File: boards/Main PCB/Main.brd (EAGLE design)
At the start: 160 x 101.3 mm, 19 parts, among them IC2 CP210X_USB_UART, X1 USB-MICROB

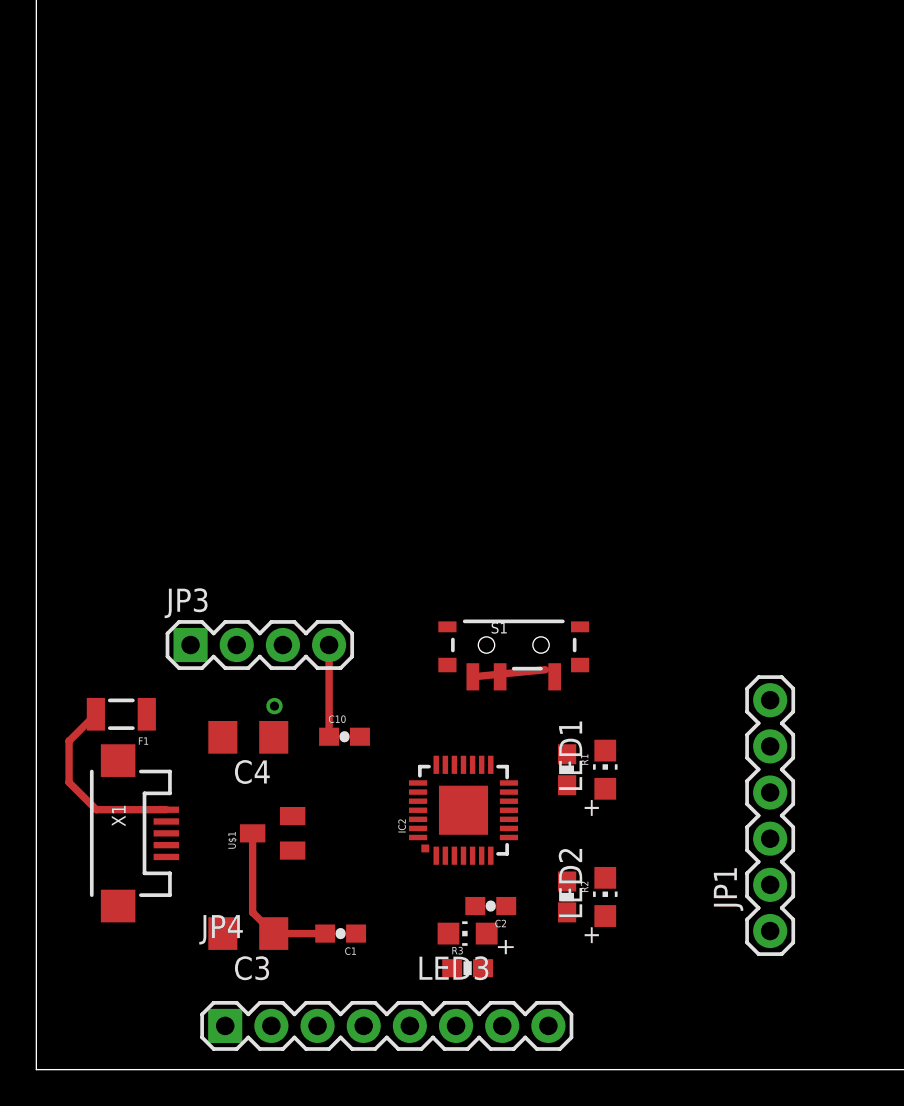
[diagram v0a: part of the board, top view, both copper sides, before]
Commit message: Adding miniusb UART converter and updating main to include IMU
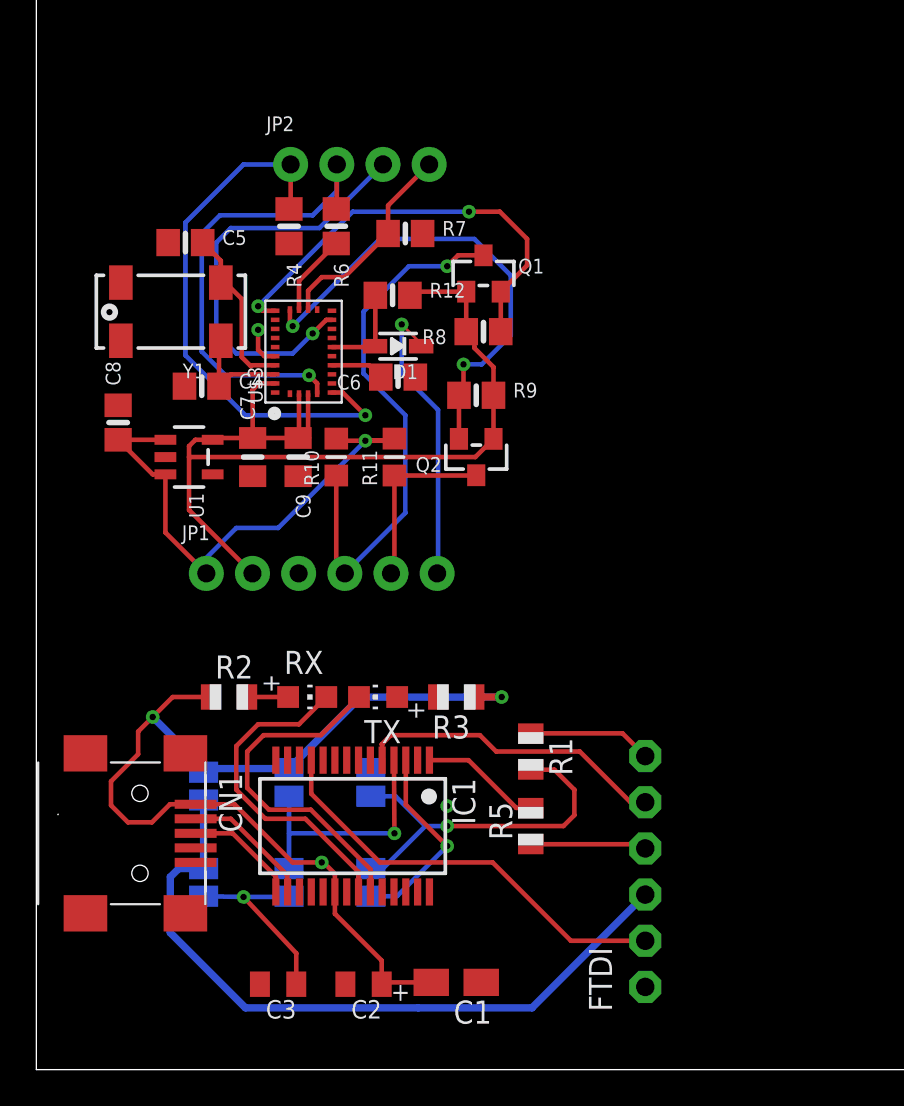
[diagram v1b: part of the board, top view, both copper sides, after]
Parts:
- removed C10: 100nF, SparkFun:0603-CAP
- removed F1: PTCSMD, SparkFun:PTC-1206
- removed IC2: CP210X_USB_UART, SparkFun-DigitalIC:MLP28
- removed JP3: (no value), SparkFun:1X04
- removed JP4: (no value), SparkFun:1X08
- removed LED1: bijela, adafruit:CHIP-LED0805
- removed LED2: crvena, adafruit:CHIP-LED0805
- removed LED3: plava, adafruit:CHIP-LED0805
- removed S1: (no value), SparkFun:SWITCH-SPST-SMD-A
- removed U$1: 622K, SparkFun:662K
- removed X1: USB-MICROB, SparkFun:USB-MICROB
- added C5: 22pF, microbuilder:0805-NO
- added C6: 0.1uF, microbuilder:0805-NO
- added C7: 0.1uF, microbuilder:0805_10MGAP
- added C8: 10uF, microbuilder:0805-NO
- added C9: 10uF, microbuilder:0805_10MGAP
- added CN1: MINIB, adafruit:USB-MINIB
- added D1: 1n4148, microbuilder:SOD-323
- added FTDI: (no value), adafruit:1X06-CLEANBIG
- added IC1: FT232RL, ftdichip:SSOP28
- added JP2: (no value), microbuilder:1X04_ROUND_76
- added Q1, Q2: BSS138, microbuilder:SOT23-WIDE
- added R10, R11: 10K, microbuilder:_0805MP
- added R12, R4, R6, R7, R8, R9: 10K, microbuilder:0805-NO
- added R5: 10, adafruit:R0805
- added RX: Green, adafruit:CHIP-LED0805
- added SJ1, SJ2, SJ3, SJ4, SJ5, SJ6: (no value), jumper:SJ
- added TX: Red, adafruit:CHIP-LED0805
- added U$3: BNO055, microbuilder:BNO055
- added U1: MIC5225-3.3, microbuilder:SOT23-5
- added Y1: 32.768kHz, microbuilder:CRYSTAL_8X3.8
- C1: value 100nF -> 10uF; device SparkFun:0603-CAP -> adafruit:A/3216-18R
- C2: value 100nF -> 0.1uF; device SparkFun:0603-CAP -> adafruit:C0805K
- C3: value 10uF -> 0.1uF; device rcl:C3216 -> adafruit:C0805K
- C4: value 22uF -> 22pF; device rcl:C3216 -> microbuilder:0805-NO
- JP1: value FTDI_BASICPTH -> (none); device SparkFun:FTDI_BASIC -> microbuilder:1X06_ROUND_76
- R1: value 680 -> 10; device SparkFun:0603-RES -> adafruit:R0805
- R2, R3: value 680 -> 1K; device SparkFun:0603-RES -> adafruit:R0805
- moved JP1 31.6 mm to (15.7, 27.3), turned to 0 degrees
- moved R2 21.6 mm to (10.6, 20.5), turned to 0 degrees
- moved C4 19.5 mm to (9.10, 37.6), turned to 0 degrees
- moved R3 14.9 mm to (23.1, 20.5), turned to 180 degrees
- moved C2 8.22 mm to (18.0, 4.70)
- moved C1 6.90 mm to (23.1, 4.80)
- moved C3 3.23 mm to (13.3, 4.70)
- moved R1 2.24 mm to (27.2, 17.5)
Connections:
- removed net D+: IC2.4, X1.D+
- removed net D-: IC2.5, X1.D-
- removed net DCD: IC2.1, JP4.4
- removed net DSR: IC2.27, JP4.3
- removed net RI: IC2.2, JP4.5
- removed net RST: IC2.9, JP4.8
- removed net RXD: IC2.25, JP1.RXI, LED2.C
- removed net SUSPEND: IC2.12, JP4.7
- removed net SUSPEND': IC2.11, JP4.6
- removed net TXD: IC2.26, JP1.TXO, LED1.C
- removed net VBUS: F1.2, X1.VBUS
- removed net VCC: JP1.VCC, S1.2
- new net +3V3: C3.1, IC1.17, SJ4.2, SJ5.2
- new net 5.0V: C8.1, JP1.1, R10.2, R11.2, U1.1, U1.3
- new net I2CADDR_3V: JP2.4, R7.1, U$3.17
- new net INT_3V: JP2.3, U$3.14
- new net N$10: C5.2, U$3.26, Y1.P$1
- new net N$11: C6.2, U$3.9
- new net N$5: IC1.1, R5.2
- new net N$6: IC1.23, TX.C
- new net N$7: IC1.22, RX.C
- new net N$8: R2.2, RX.A
- new net N$9: R3.2, TX.A
- new net NRESET_3V: D1.A, R12.1, U$3.11
- new net PS0_3V: JP2.1, R4.1, U$3.6
- new net PS1_3V: JP2.2, R6.1, U$3.5
- new net RST_5V: D1.C, JP1.6
- new net RTSDTR: R1.2, SJ3.2, SJ6.1
- new net RX: FTDI.5, IC1.5
- new net SCL_3V: Q2.2, R9.1, U$3.19
- new net SCL_5V: JP1.5, Q2.3, R11.1
- new net SDA_3V: Q1.2, R8.1, U$3.20
- new net SDA_5V: JP1.4, Q1.3, R10.1
- new net TX: FTDI.4, R5.1
- new net VCCIO: IC1.4, SJ2.2, SJ5.1
- new net VCCOUT: FTDI.3, SJ1.2, SJ4.1
- net +5V: now also C1.+, C2.1, CN1.VBUS, IC1.20, SJ1.1, SJ2.1; no longer C1.2, C3.1, F1.1, IC2.7, IC2.8, JP3.3, R1.1, S1.1, U$1.IN
- net 3.3V: now also C7.2, C9.1, JP1.2, Q1.1, Q2.1, R12.2, R8.2, R9.2, U$3.28, U$3.3, U$3.4, U1.5; no longer C10.1, C4.1, JP3.4, S1.3, U$1.OUT
- net CTS: now also FTDI.2, IC1.11; no longer IC2.23, JP1.CTS, JP4.1
- net DTR: now also IC1.2, SJ6.2; no longer IC2.28, JP1.DTR
- net GND: now also C1.-, C4.1, C5.1, C6.1, C7.1, C8.2, C9.2, CN1.GND, FTDI.1, IC1.18, IC1.21, IC1.25, IC1.26, IC1.7, JP1.3, R4.2, R6.2, R7.2, U$3.10, U$3.15, U$3.16, U$3.18, U$3.2, U$3.25, U1.2; no longer C1.1, C10.2, C4.2, IC2.3, IC2.EXP, IC2.M, JP1.GND, JP3.1, JP3.2, LED3.C, U$1.GND, X1.GND
- net N$1: now also C4.2, U$3.27, Y1.P$4; no longer LED1.A, R1.2
- net N$2: now also FTDI.6, R1.1; no longer LED2.A, R2.2
- net N$3: now also CN1.D+, IC1.15; no longer LED3.A, R3.2
- net N$4: now also CN1.D-, IC1.16; no longer C2.1, IC2.6
- net RTS: now also IC1.3, SJ3.1; no longer IC2.24, JP4.2
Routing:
- net 3.3V: track 5.05 -> 53.2 mm
- net +5V: track 12.8 -> 57.9 mm, vias 0 -> 3
- net VCCOUT: track 0.00 -> 39.3 mm
- net PS0_3V: track 0.00 -> 30.5 mm, vias 0 -> 1
- net SDA_5V: track 0.00 -> 30.2 mm, vias 0 -> 1
- net 5.0V: track 0.00 -> 29.2 mm, vias 0 -> 1
- net SCL_3V: track 0.00 -> 26.6 mm, vias 0 -> 2
- net PS1_3V: track 0.00 -> 26.5 mm, vias 0 -> 1
- net SDA_3V: track 0.00 -> 24.3 mm, vias 0 -> 2
- net CTS: track 0.00 -> 23.6 mm
- net INT_3V: track 0.00 -> 23.5 mm, vias 0 -> 1
- net RTSDTR: track 0.00 -> 20.4 mm, vias 0 -> 1
- net N$6: track 0.00 -> 19.3 mm
- net N$7: track 0.00 -> 18.2 mm
- net RX: track 0.00 -> 17.1 mm
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
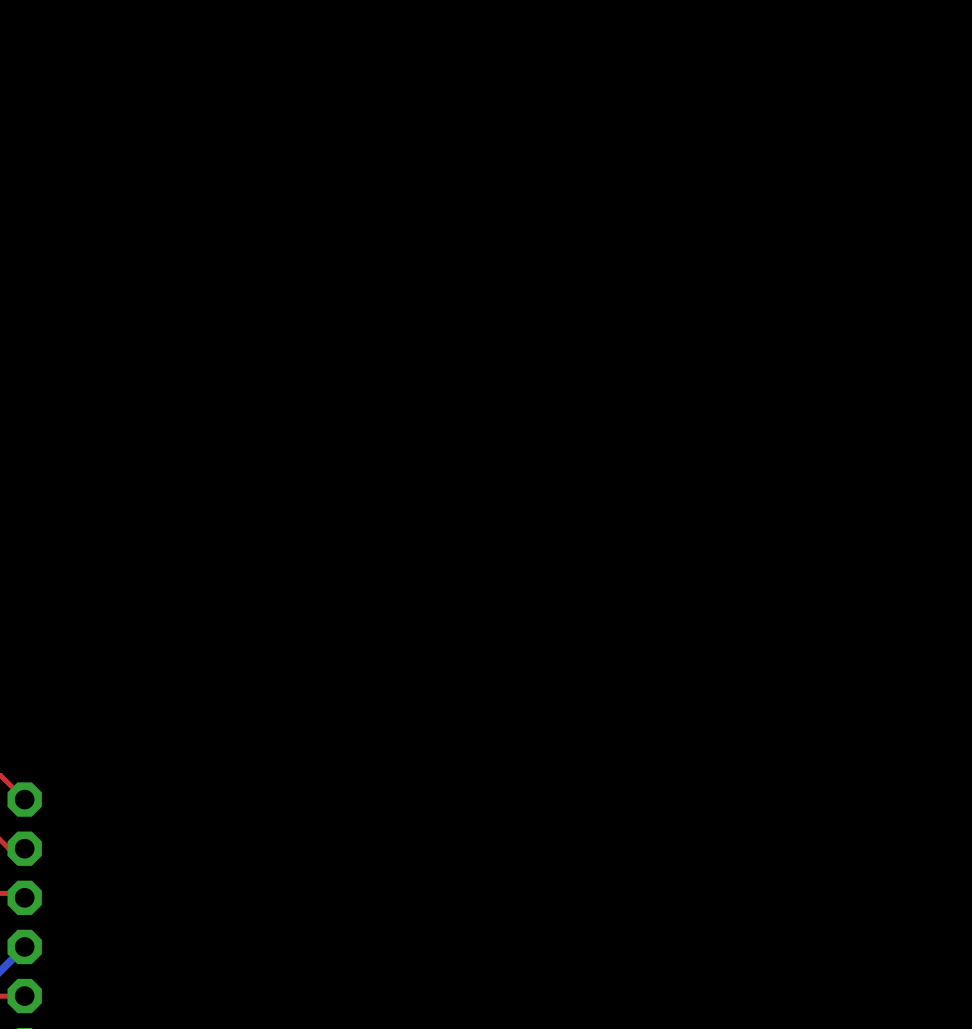
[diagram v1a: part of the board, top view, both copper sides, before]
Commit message: Fixing NS-HP-GL library and importing footprint to main PCB
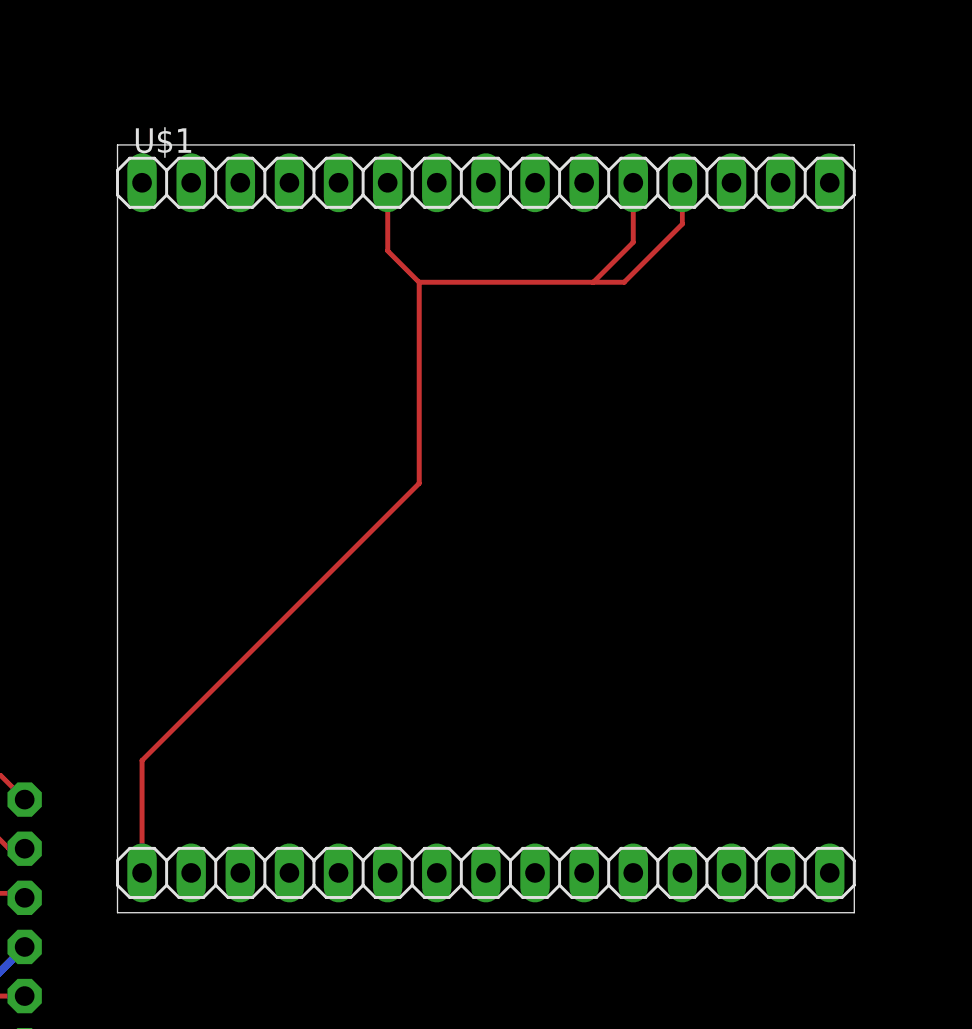
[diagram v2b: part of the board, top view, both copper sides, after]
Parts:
- added U$1: GPS, NS-HP-GL:GPS
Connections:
- new net RX1: U$1.19
- new net RX2: U$1.22
- new net TX1: U$1.20
- new net TX2: U$1.21
- net +3V3: now also U$1.11, U$1.12, U$1.16, U$1.6
- net GND: now also U$1.1, U$1.13, U$1.15, U$1.17, U$1.26, U$1.27
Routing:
- net +3V3: track 10.7 -> 76.0 mm
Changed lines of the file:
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@@
 <?xml version="1.0" encoding="utf-8"?>
 <!DOCTYPE eagle SYSTEM "eagle.dtd">
-<eagle version="9.2.2">
+<eagle version="9.3.0">
 <drawing>
 <settings>
@@
 <attribute name="VALUE" x="21" y="41.592" size="0.4064" layer="27" ratio="10" rot="R180"/>
 </element>
+<element name="U$1" library="NS-HP-GL" package="GPS" value="GPS" x="38.3" y="11.4" smashed="yes">
+<attribute name="NAME" x="38.2238" y="15.6672" size="1.27" layer="25" ratio="10"/>
+<attribute name="NAME" x="39.1128" y="50.6938" size="1.27" layer="25" ratio="10"/>
+<attribute name="VALUE" x="38.3" y="10.765" size="1.27" layer="27"/>
+<attribute name="VALUE" x="38.935" y="46.7314" size="1.27" layer="27"/>
+</element>
 </elements>
 <signals>
@@
 <wire x1="16.5" y1="45.45" x2="14.45" y2="43.4" width="0.254" layer="1"/>
 <wire x1="14.45" y1="43.4" x2="14.45" y2="41.8125" width="0.254" layer="1"/>
+<contactref element="U$1" pad="13"/>
+<contactref element="U$1" pad="15"/>
+<contactref element="U$1" pad="17"/>
+<contactref element="U$1" pad="27"/>
+<contactref element="U$1" pad="26"/>
+<contactref element="U$1" pad="1"/>
+<wire x1="70.05" y1="49.1444" x2="75.13" y2="49.1444" width="0" layer="19" extent="1-1"/>
+<wire x1="39.57" y1="49.1444" x2="70.05" y2="49.1444" width="0" layer="19" extent="1-1"/>
+<wire x1="21.25" y1="46" x2="39.57" y2="49.1444" width="0" layer="19" extent="1-1"/>
 <wire x1="16.5" y1="45.45" x2="21.25" y2="46" width="0" layer="19" extent="1-1"/>
 <wire x1="15.45" y1="41.8125" x2="14.45" y2="41.8125" width="0" layer="19" extent="1-1"/>
@@
 <wire x1="8.764" y1="11.4" x2="15.125" y2="9.775" width="0" layer="19" extent="1-1"/>
 <wire x1="33.5" y1="4.55" x2="24.475" y2="4.8" width="0" layer="19" extent="1-1"/>
+<wire x1="42.11" y1="13.4574" x2="33.5" y2="4.55" width="0" layer="19" extent="1-1"/>
+<wire x1="64.97" y1="13.4574" x2="42.11" y2="13.4574" width="0" layer="19" extent="1-1"/>
+<wire x1="67.51" y1="13.4574" x2="64.97" y2="13.4574" width="0" layer="19" extent="1-1"/>
 </signal>
 <signal name="N$3">
@@
 <wire x1="11.4" y1="9.5" x2="14.3" y2="6.4" width="0.254" layer="1"/>
 <wire x1="14.3" y1="6.4" x2="14.3" y2="4.7" width="0.254" layer="1"/>
+<contactref element="U$1" pad="6"/>
+<contactref element="U$1" pad="16"/>
+<contactref element="U$1" pad="12"/>
+<contactref element="U$1" pad="11"/>
+<wire x1="52.27" y1="49.1444" x2="52.27" y2="45.63" width="0.254" layer="1"/>
+<wire x1="53.9" y1="44" x2="62.9" y2="44" width="0.254" layer="1"/>
+<wire x1="62.9" y1="44" x2="64.97" y2="46.07" width="0.254" layer="1"/>
+<wire x1="64.97" y1="46.07" x2="64.97" y2="49.1444" width="0.254" layer="1"/>
+<wire x1="52.27" y1="45.63" x2="53.9" y2="44" width="0.254" layer="1"/>
+<wire x1="67.51" y1="49.1444" x2="67.51" y2="47.01" width="0.254" layer="1"/>
+<wire x1="67.51" y1="47.01" x2="64.5" y2="44" width="0.254" layer="1"/>
+<wire x1="64.5" y1="44" x2="62.9" y2="44" width="0.254" layer="1"/>
+<wire x1="53.9" y1="44" x2="53.9" y2="33.6" width="0.254" layer="1"/>
+<wire x1="39.57" y1="19.27" x2="39.57" y2="13.4574" width="0.254" layer="1"/>
+<wire x1="53.9" y1="33.6" x2="39.57" y2="19.27" width="0.254" layer="1"/>
+<wire x1="14.475" y1="9.775" x2="39.57" y2="13.4574" width="0" layer="19" extent="1-1"/>
 <wire x1="13.9" y1="9.538" x2="14.475" y2="9.775" width="0" layer="19" extent="1-16"/>
 </signal>
@@
 <wire x1="22.1" y1="27.35" x2="22.05" y2="27.3" width="0.1524" layer="16"/>
 </signal>
+<signal name="RX1">
+<contactref element="U$1" pad="19"/>
+</signal>
+<signal name="TX1">
+<contactref element="U$1" pad="20"/>
+</signal>
+<signal name="TX2">
+<contactref element="U$1" pad="21"/>
+</signal>
+<signal name="RX2">
+<contactref element="U$1" pad="22"/>
+</signal>
 </signals>

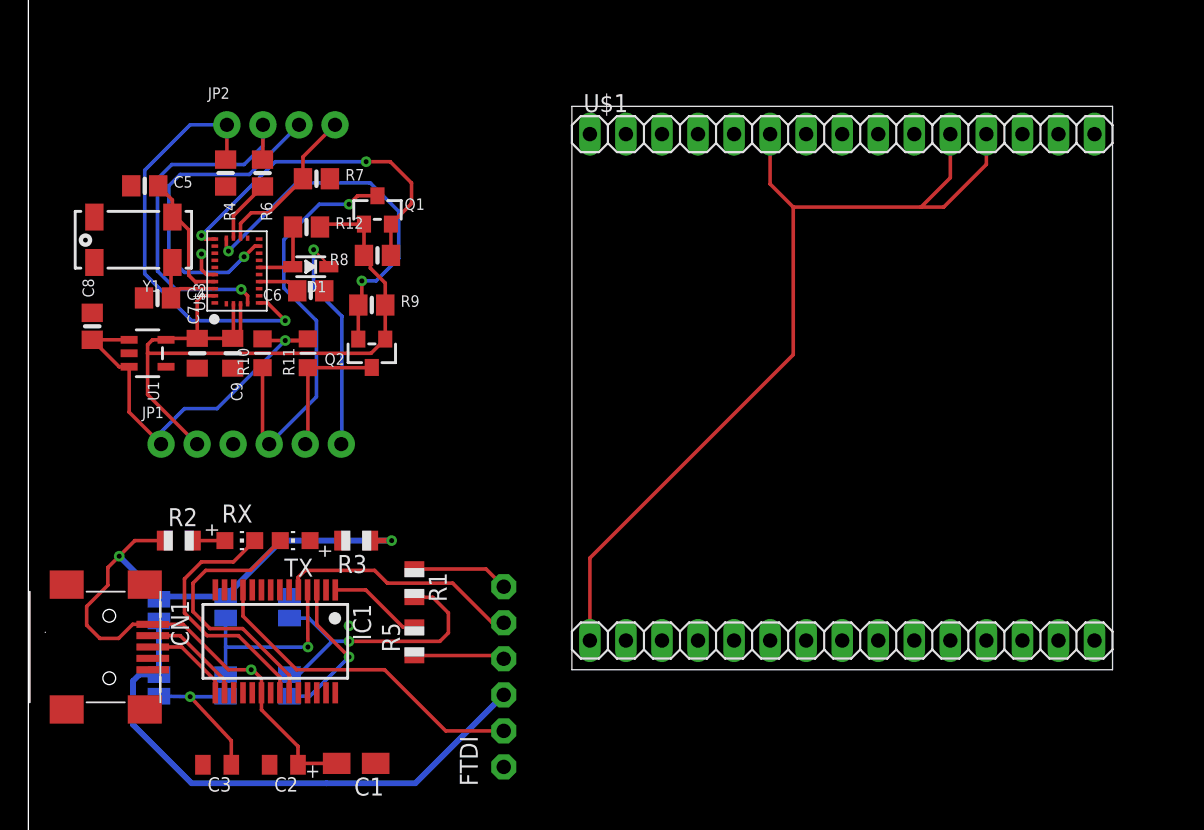
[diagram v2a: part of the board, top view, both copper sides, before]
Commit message: Cleaning up PCB folders aand updating proper dimensioned GPS chip
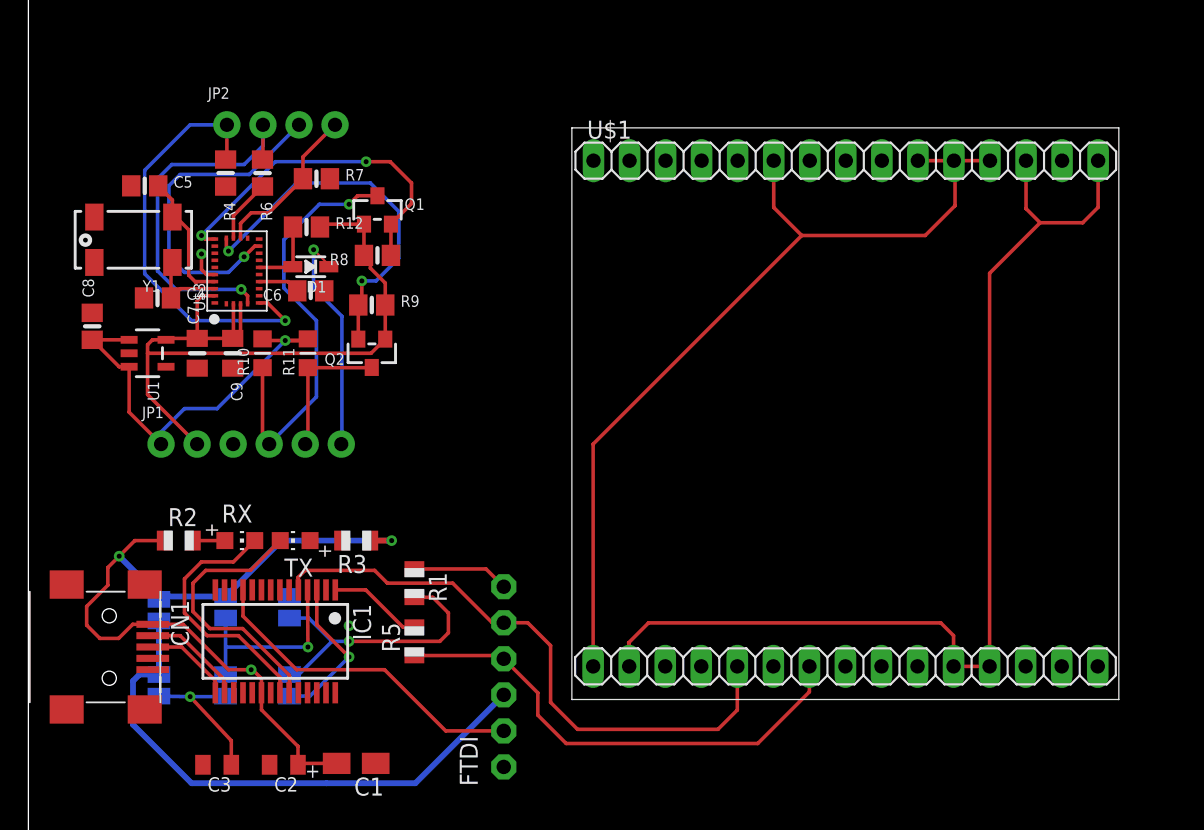
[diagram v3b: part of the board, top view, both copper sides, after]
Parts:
- moved U$1 2.10 mm to (38.3, 9.30)
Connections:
- removed net RX1: U$1.19
- removed net RX2: U$1.22
- removed net TX1: U$1.20
- removed net TX2: U$1.21
- net +3V3: now also U$1.10
- net RX: now also U$1.20
- net TX: now also U$1.22
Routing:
- net GND: track 6.67 -> 82.3 mm
- net TX: track 6.40 -> 34.6 mm
- net RX: track 17.1 -> 42.7 mm
- net +3V3: track 76.0 -> 73.2 mm
